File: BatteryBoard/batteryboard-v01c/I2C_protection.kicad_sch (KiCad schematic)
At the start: 22 parts

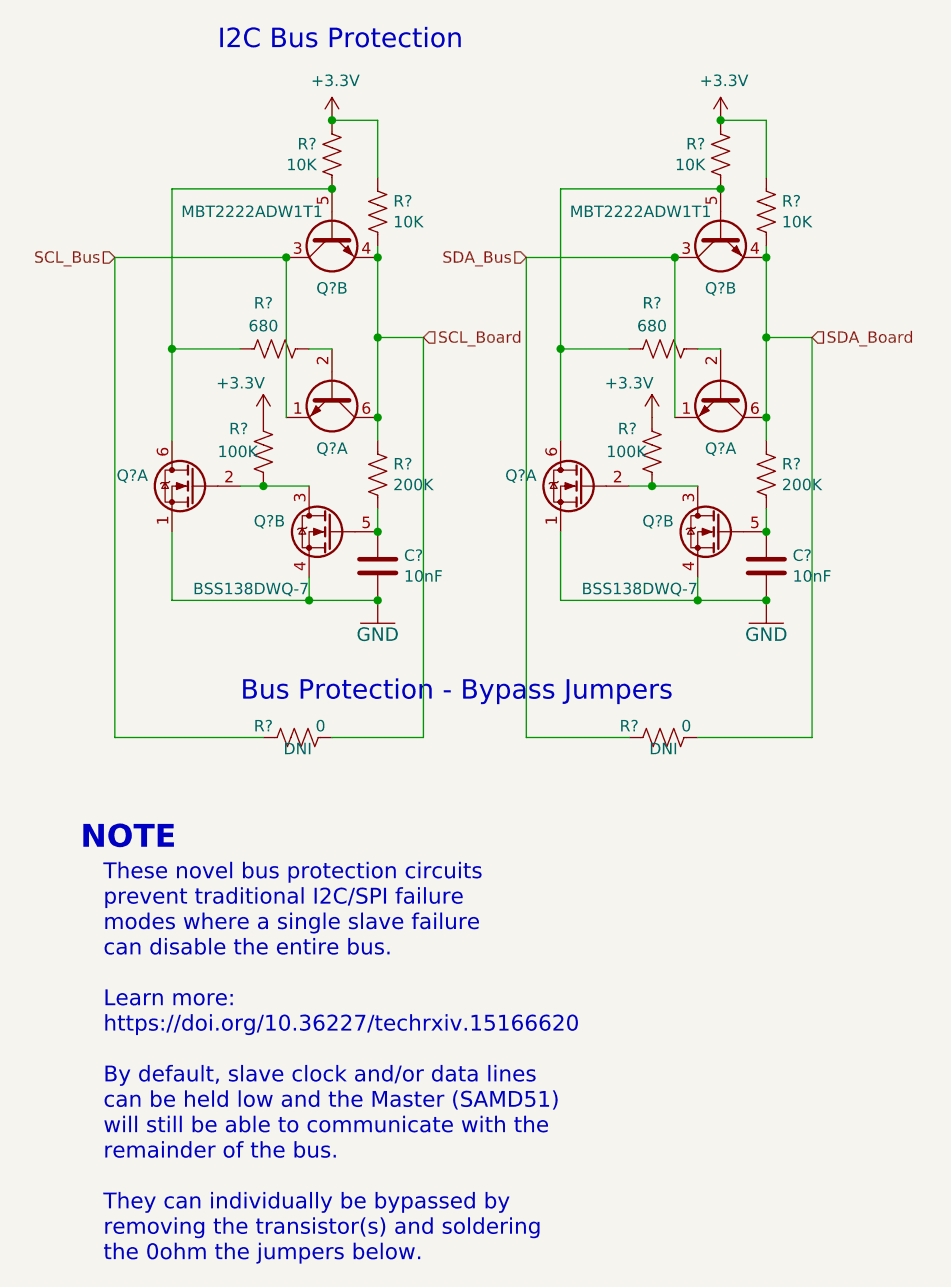
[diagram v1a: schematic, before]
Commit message: Fixed some battery board 3Dmodels
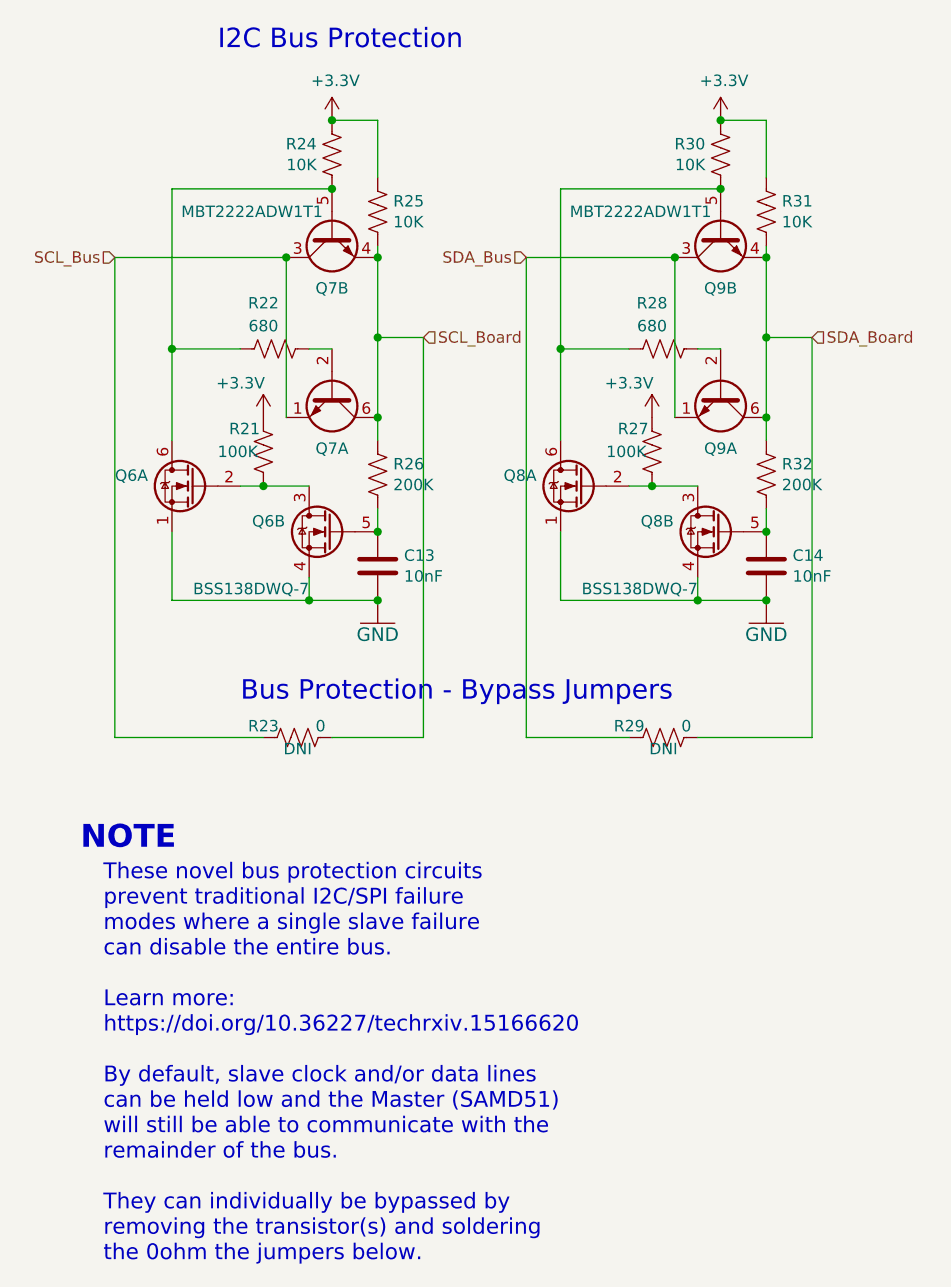
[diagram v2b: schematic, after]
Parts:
- gave numbers to parts that had none: 18
